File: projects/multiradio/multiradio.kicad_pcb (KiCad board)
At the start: 2 copper layers, 155 x 115 mm, 21 parts, among them J1 USB_B

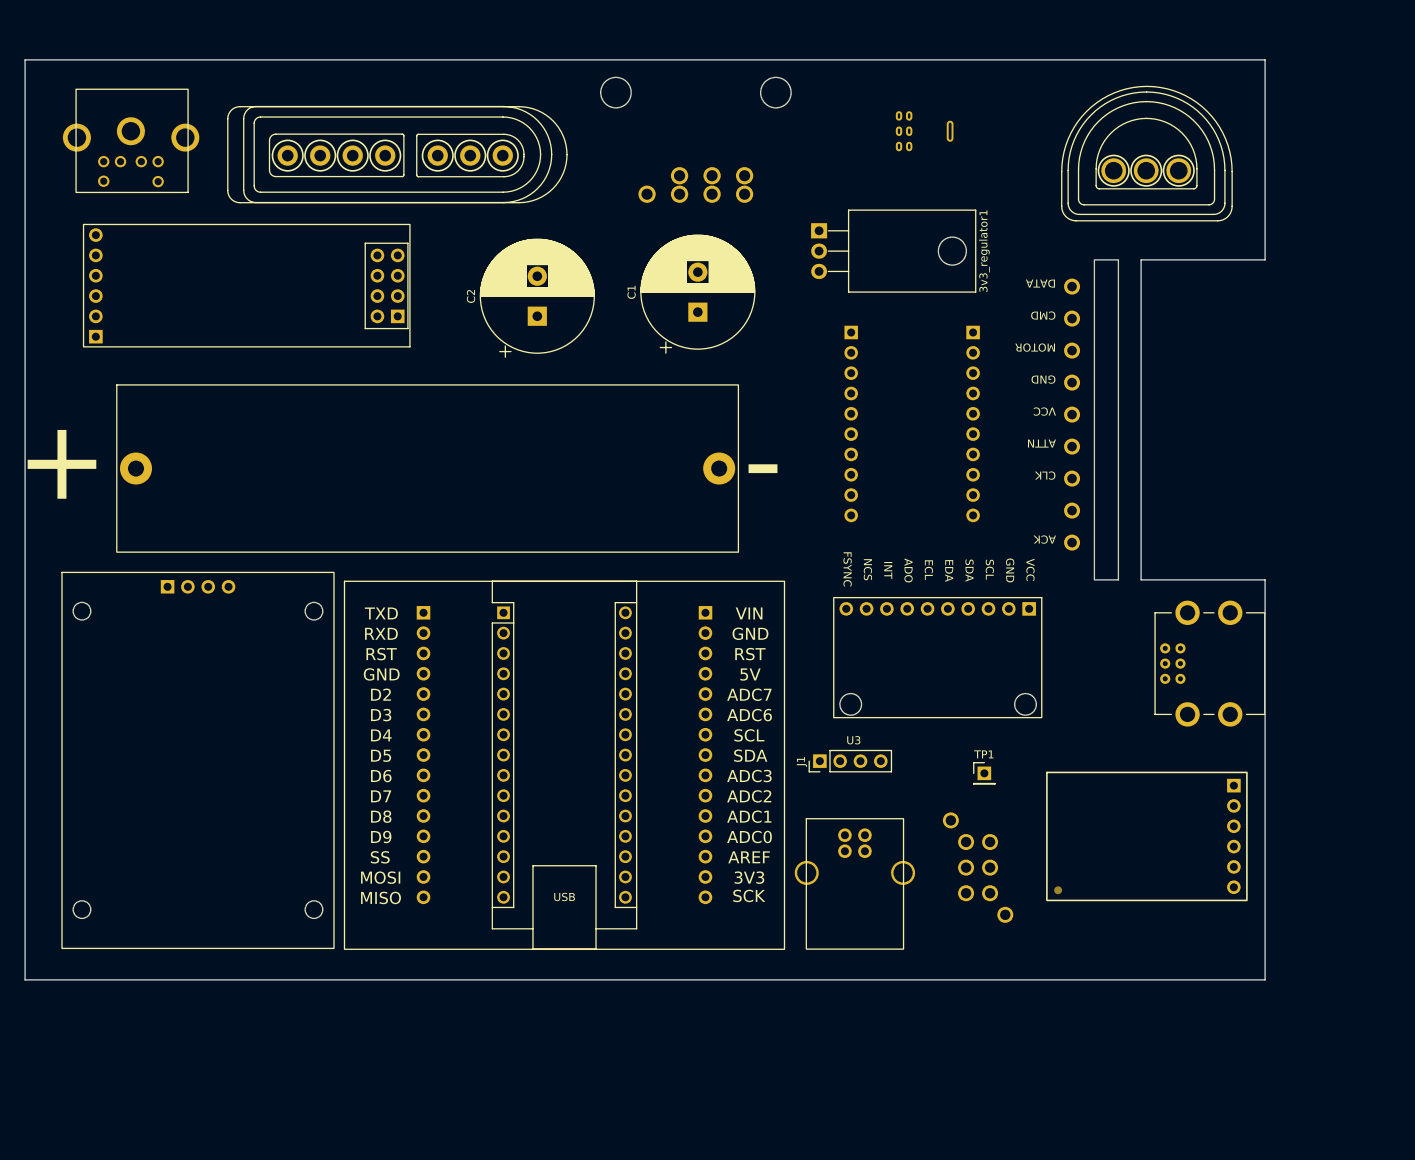
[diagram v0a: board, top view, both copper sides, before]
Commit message: update to 3.3v bat radio
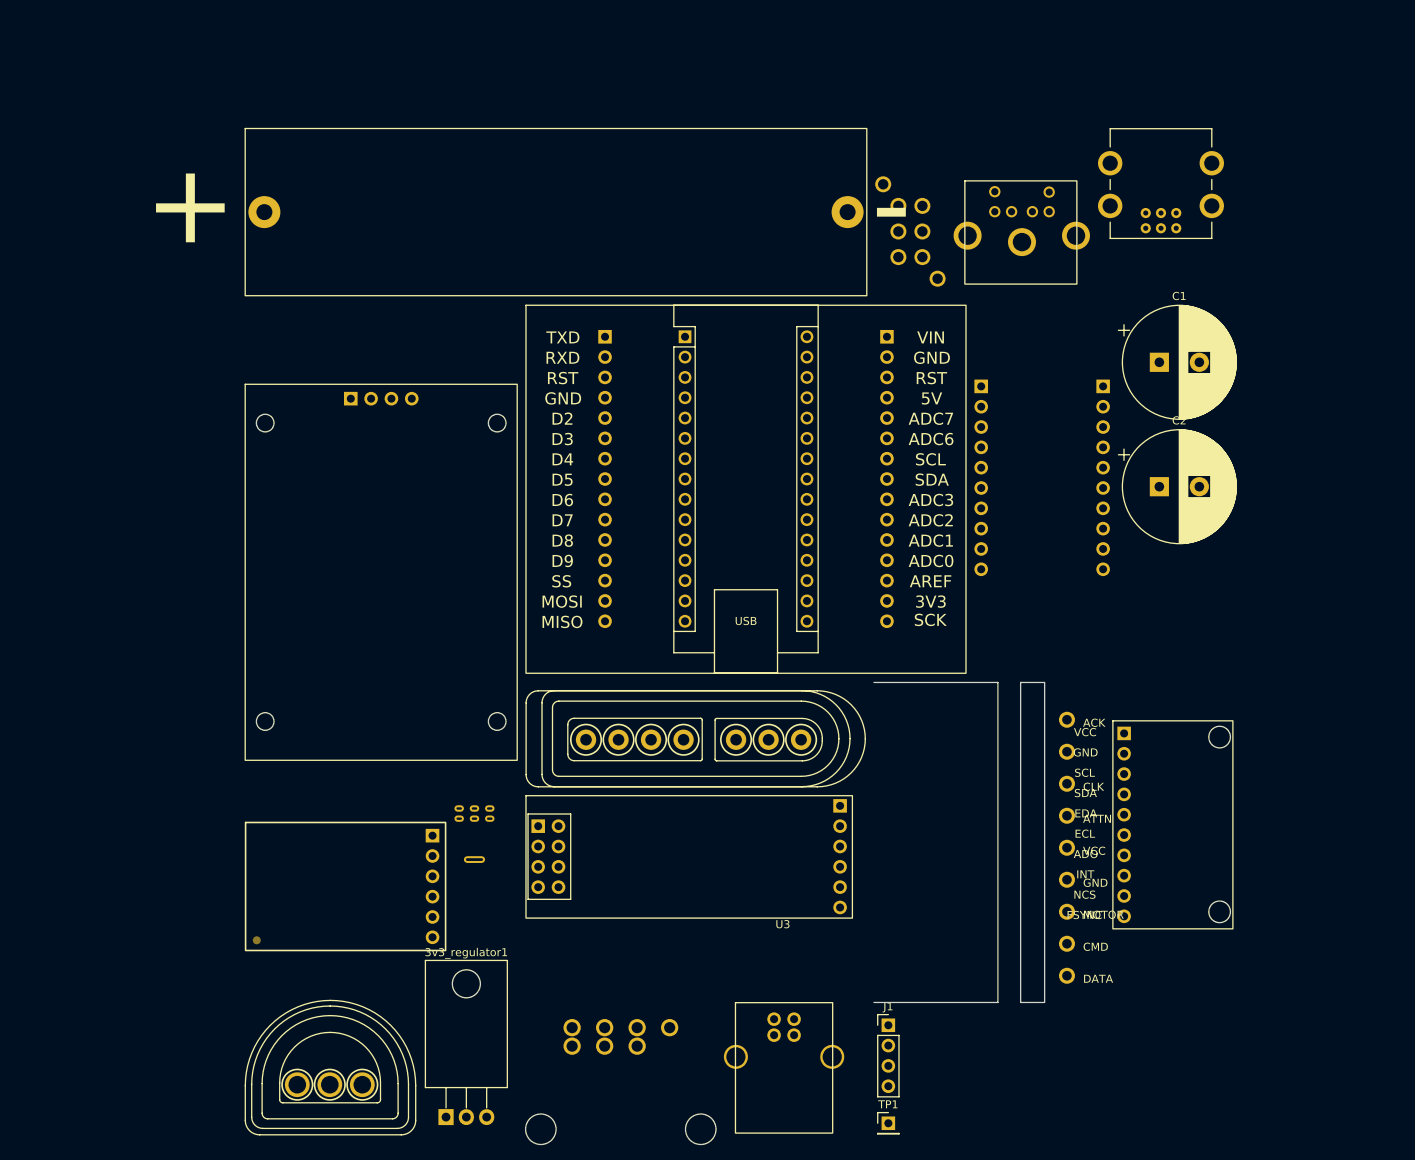
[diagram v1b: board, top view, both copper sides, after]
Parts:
- moved N64_controller1 153.2 mm to (72.8, 146.2)
- moved 3v3_regulator1 120.2 mm to (87.4, 165.7), turned to 0 degrees
- moved ps/2_connector1 112.3 mm to (159.4, 42.3), turned to 0 degrees
- moved U1 100.4 mm to (74.3, 122.3)
- moved Gamecube1 93.4 mm to (90.9, 122.3), turned to 0 degrees
- moved Snes1 82.0 mm to (117.4, 111.5)
- moved C2 80.6 mm to (176.6, 86.9), turned to 0 degrees
- moved Nes1 80.5 mm to (107.2, 142.1), turned to 0 degrees
- moved U5 80.0 mm to (145.3, 42.3)
- moved NRF1 66.1 mm to (98.9, 129.3), turned to 0 degrees
- moved wii1 60.3 mm to (176.8, 49.0), turned to 0 degrees
- moved C1 58.0 mm to (176.6, 71.3), turned to 0 degrees
- moved Playstation1 48.2 mm to (169.5, 128.7), turned to 0 degrees
- moved TP1 45.4 mm to (142.7, 166.4)
- moved A1 41.3 mm to (117.3, 68.1)
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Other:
- board size 155 x 115 mm -> 21.3 x 40 mm

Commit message: ps2 180 degree
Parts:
- Playstation1: footprint Footprints_cez:Playstation 2 controller 90 degree -> Footprints_cez:Playstation 2 controller 180
- U2: footprint Footprints_cez:TXS0108E -> Footprints_cez:8 Channel Logic Level Converter
- moved U3 125.1 mm to (185.6, 30.3)
- moved ps/2_connector1 106.9 mm to (119.8, 141.5)
- moved U1 106.1 mm to (177.9, 99.5)
- moved TP1 105.0 mm to (160.8, 62.9)
- moved U5 100.0 mm to (133.6, 141.5)
- moved J1 92.2 mm to (156.2, 62.9)
- moved MPU1 89.9 mm to (138.9, 30.3)
- moved Gamecube1 85.5 mm to (150.7, 61.4)
- moved Playstation1 85.3 mm to (177.0, 43.7)
- moved U2 61.9 mm to (111.5, 99.5)
- moved Nes1 61.0 mm to (151.0, 99.5)
- moved U4 60.4 mm to (120.0, 80.0)
- moved Snes1 54.6 mm to (161.1, 144.2)
- moved NRF1 43.8 mm to (142.7, 131.4)
- moved C1 41.1 mm to (153.5, 37.3)
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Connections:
- A1 pad 7: unconnected-(A1-D4-Pad7) -> Net-(A1-D4)
- A1 pad 8: unconnected-(A1-D5-Pad8) -> Net-(A1-D5)
- A1 pad 9: unconnected-(A1-D6-Pad9) -> Net-(A1-D6)
- C1 pad 1: Net-(3v3_regulator1-VO) -> Net-(3v3_regulator1-VI)
- C2 pad 1: Net-(3v3_regulator1-VI) -> Net-(3v3_regulator1-VO)
- Display1 pad 1: Net-(Display1-SDA) -> Net-(A1-A4)
- Display1 pad 2: Net-(Display1-SCL) -> Net-(A1-A5)
- Display1 pad 4: Net-(3v3_regulator1-VO) -> Net-(3v3_regulator1-VI)
- NRF1 pad 2: Net-(3v3_regulator1-VO) -> Net-(3v3_regulator1-VI)
- Nes1 pad 2: Net-(Nes1-CLK) -> Net-(A1-D8)
- Nes1 pad 3: Net-(Nes1-LTCH) -> Net-(A1-D7)
- Nes1 pad 4: Net-(Nes1-DATA) -> Net-(A1-D6)
- Playstation1 pad 4: Net-(3v3_regulator1-GND) -> unconnected-(Playstation1-GND-Pad4)
- Playstation1 pad 5: Net-(3v3_regulator1-VO) -> unconnected-(Playstation1-3.3V-Pad5)
- Snes1 pad 2: Net-(Nes1-CLK) -> Net-(A1-D8)
- Snes1 pad 3: Net-(Nes1-LTCH) -> Net-(A1-D7)
- Snes1 pad 4: Net-(Nes1-DATA) -> Net-(A1-D6)
- U2 pad 1: Net-(3v3_regulator1-VO) -> Net-(U2-LV1)
- U2 pad 10: Net-(3v3_regulator1-VO) -> Net-(Playstation1-ATTN)
- U2 pad 11: unconnected-(U2-VCC_HIGH-Pad11) -> Net-(A1-A4)
- U2 pad 12: Net-(Display1-SCL) -> Net-(A1-A5)
- U2 pad 13: Net-(Display1-SDA) -> Net-(A1-D5)
- U2 pad 14: Net-(Gamecube1-DATA) -> Net-(A1-D4)
- U2 pad 15: Net-(N64_controller1-DATA) -> Net-(3v3_regulator1-VI)
- U2 pad 16: Net-(Playstation1-ATTN) -> Net-(3v3_regulator1-GND)
- U2 pad 17: Net-(Playstation1-CMD) -> Net-(A1-D11)
- U2 pad 18: Net-(Playstation1-DATA) -> Net-(A1-D12)
- U2 pad 19: Net-(Playstation1-CLK) -> Net-(A1-D13)
- U2 pad 2: Net-(A1-A5) -> Net-(U2-LV2)
- U2 pad 20: Net-(3v3_regulator1-GND) -> Net-(A1-D10)
- U2 pad 3: Net-(A1-A4) -> Net-(N64_controller1-DATA)
- U2 pad 4: Net-(A1-D8) -> Net-(Gamecube1-DATA)
- U2 pad 5: Net-(A1-D7) -> Net-(3v3_regulator1-VO)
- U2 pad 6: Net-(A1-D10) -> Net-(3v3_regulator1-GND)
- U2 pad 7: Net-(A1-D11) -> Net-(Playstation1-CMD)
- U2 pad 8: Net-(A1-D12) -> Net-(Playstation1-DATA)
- U2 pad 9: Net-(A1-D13) -> Net-(Playstation1-CLK)
- wii1 pad 2: Net-(Display1-SCL) -> Net-(U2-LV2)
- wii1 pad 5: Net-(Display1-SDA) -> Net-(U2-LV1)
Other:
- board outline removed

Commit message: multiremote done
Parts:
- removed J1: USB_B, Connector_PinHeader_2.54mm:PinHeader_1x04_P2.54mm_Vertical
- removed TP1: TestPoint, Connector_PinHeader_2.54mm:PinHeader_1x01_P2.54mm_Vertical
- removed U1: ~, Footprints_cez:MH-CD42
- removed U3: ~, Footprints_cez:USB-B
- removed U4: ~, Footprints_cez:BH-18650-PC2
- removed U5: ~, Footprints_cez:Switch A03 PS-22F03
- added REF**: MountingHole_3.2mm_M3, MountingHole:MountingHole_3.2mm_M3, F.Cu at (175.3, 51.8)
- added REF**: MountingHole_3.2mm_M3, MountingHole:MountingHole_3.2mm_M3, F.Cu at (99.8, 107.4)
- added REF**: MountingHole_3.2mm_M3, MountingHole:MountingHole_3.2mm_M3, F.Cu at (88.6, 59.2)
- added REF**: MountingHole_3.2mm_M3, MountingHole:MountingHole_3.2mm_M3, F.Cu at (199.9, 76.2)
- added REF**: MountingHole_3.2mm_M3, MountingHole:MountingHole_3.2mm_M3, F.Cu at (177.5, 124.0)
- moved N64_controller1 128.1 mm to (206.1, 89.1), turned to -90 degrees
- moved ps/2_connector1 100.8 mm to (167.6, 52.8), turned to 180 degrees
- moved Snes1 95.4 mm to (134.6, 52.5), turned to 180 degrees
- moved 3v3_regulator1 84.8 mm to (128.5, 74.8)
- moved U2 77.6 mm to (188.3, 110.5), turned to 180 degrees
- moved A1 71.0 mm to (123.8, 99.4), turned to -90 degrees
- moved wii1 66.1 mm to (190.6, 129.8), turned to 180 degrees
- moved Nes1 64.2 mm to (97.3, 64.3), turned to 180 degrees
- moved NRF1 62.5 mm to (121.0, 72.8), turned to 180 degrees
- moved Gamecube1 59.0 mm to (190.6, 105.0)
- moved MPU1 58.8 mm to (127.2, 87.9), turned to 90 degrees
- moved Display1 49.1 mm to (122.0, 117.5), turned to 90 degrees
- moved C1 27.3 mm to (169.2, 59.7), turned to 180 degrees
- moved Playstation1 18.9 mm to (194.2, 51.6)
- moved C2 16.1 mm to (144.3, 66.0)
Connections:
- NRF1 pad 2: Net-(3v3_regulator1-VI) -> Net-(3v3_regulator1-VO)
- Playstation1 pad 4: unconnected-(Playstation1-GND-Pad4) -> Net-(3v3_regulator1-GND)
- Playstation1 pad 5: unconnected-(Playstation1-3.3V-Pad5) -> Net-(3v3_regulator1-VO)
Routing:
- net Net-(3v3_regulator1-GND): track 0.00 -> 400.4 mm
- net Net-(3v3_regulator1-VI): track 0.00 -> 280.7 mm
- net Net-(3v3_regulator1-VO): track 0.00 -> 161.9 mm
- net Net-(A1-D13): track 0.00 -> 146.7 mm
- net Net-(A1-D3): track 0.00 -> 143.6 mm
- net Net-(A1-D2): track 0.00 -> 138.1 mm
- net Net-(A1-D11): track 0.00 -> 120.1 mm
- net Net-(A1-D12): track 0.00 -> 117.0 mm
- net Net-(A1-D8): track 0.00 -> 104.4 mm
- net Net-(A1-D10): track 0.00 -> 97.1 mm
- net Net-(A1-D7): track 0.00 -> 95.0 mm
- net Net-(A1-A4): track 0.00 -> 94.2 mm
- net Net-(A1-A5): track 0.00 -> 91.1 mm
- net Net-(A1-D6): track 0.00 -> 85.6 mm
- net Net-(A1-D5): track 0.00 -> 72.9 mm
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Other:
- board outline added: 125 x 105 mm

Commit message: and to the factory it goes
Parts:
- added REF**: MountingHole_3.2mm_M3, MountingHole:MountingHole_3.2mm_M3, F.Cu at (84.3, 132.3)
- added REF**: MountingHole_3.2mm_M3, MountingHole:MountingHole_3.2mm_M3, F.Cu at (84.3, 82.0)
- moved REF** 32.7 mm to (200.4, 100.6)
- moved REF** 6.60 mm to (106.4, 107.4)
- moved REF** 0.72 mm to (200.4, 76.7)
- moved REF** 0.72 mm to (174.8, 51.3)
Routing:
- net Net-(A1-D13): track 146.7 -> 147.6 mm
- net Net-(A1-D12): track 117.0 -> 117.6 mm
- net Net-(A1-D11): track 120.1 -> 120.7 mm
